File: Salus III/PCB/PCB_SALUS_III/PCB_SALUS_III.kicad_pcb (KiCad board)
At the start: 2 copper layers, 200 x 140 mm, 47 parts, among them J1 Conn_01x20_Pin, J2 Conn_01x20_Pin, K1 Relay_SPDT, U1 ESP32-DEVKITC-32D

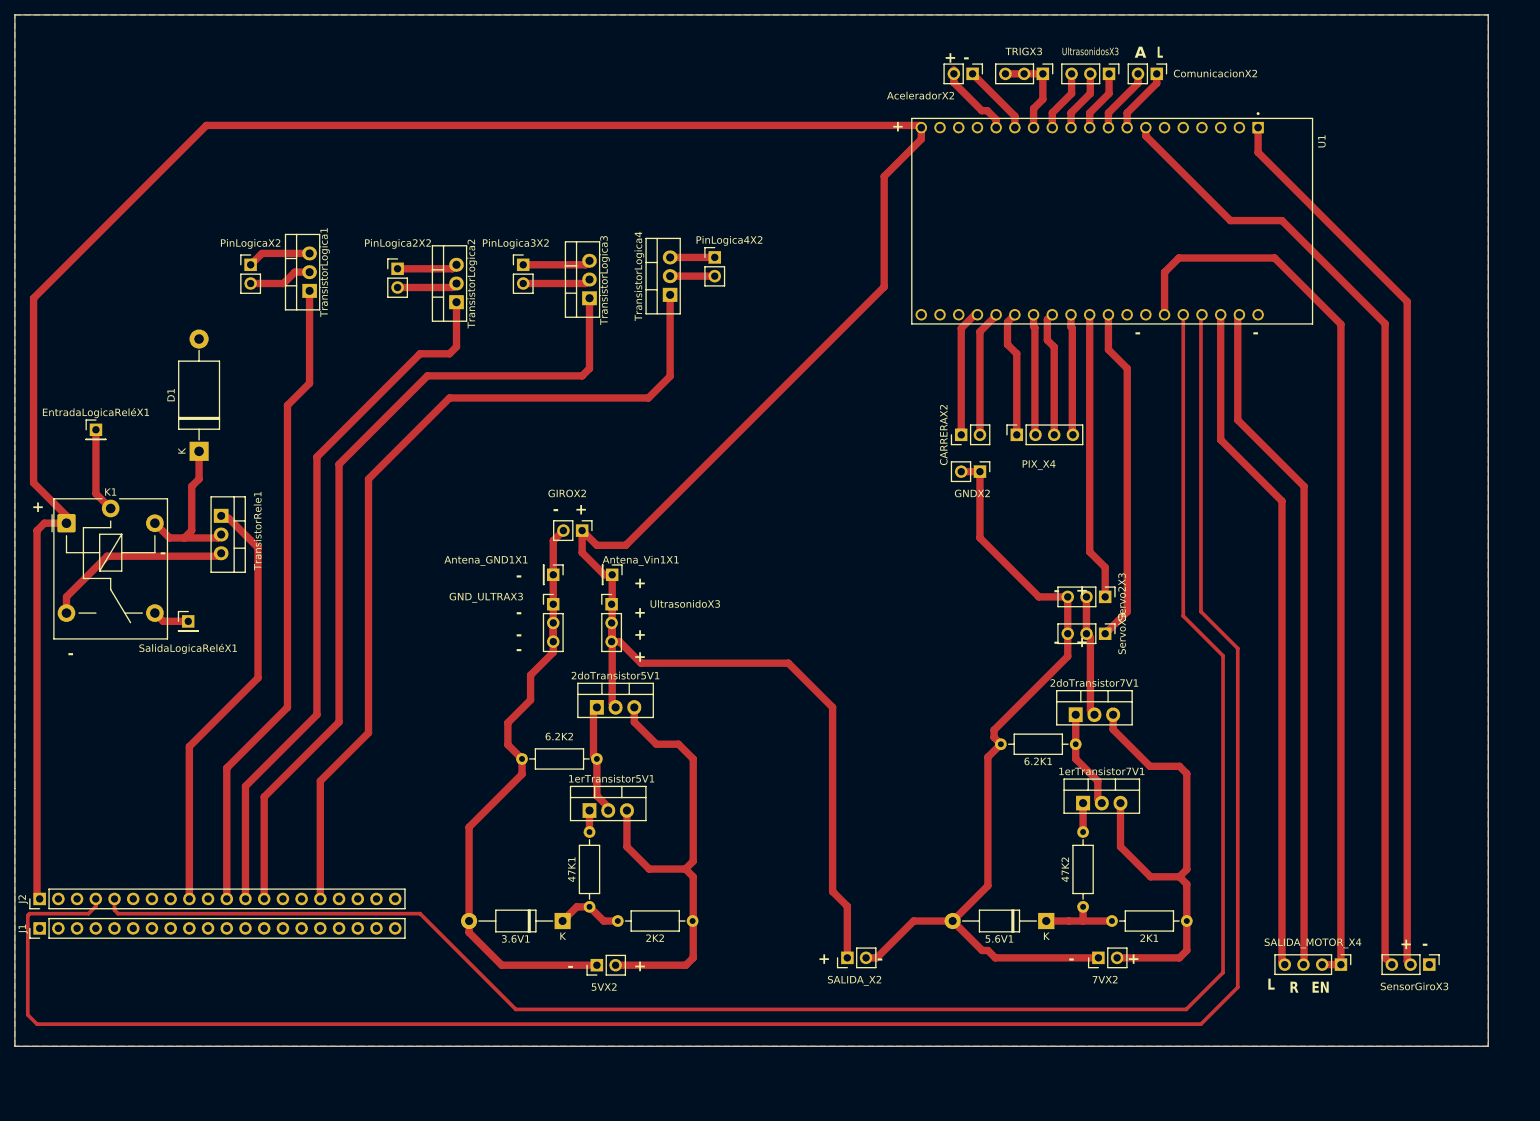
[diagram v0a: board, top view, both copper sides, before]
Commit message: Cambios para realizarla en acido preparados
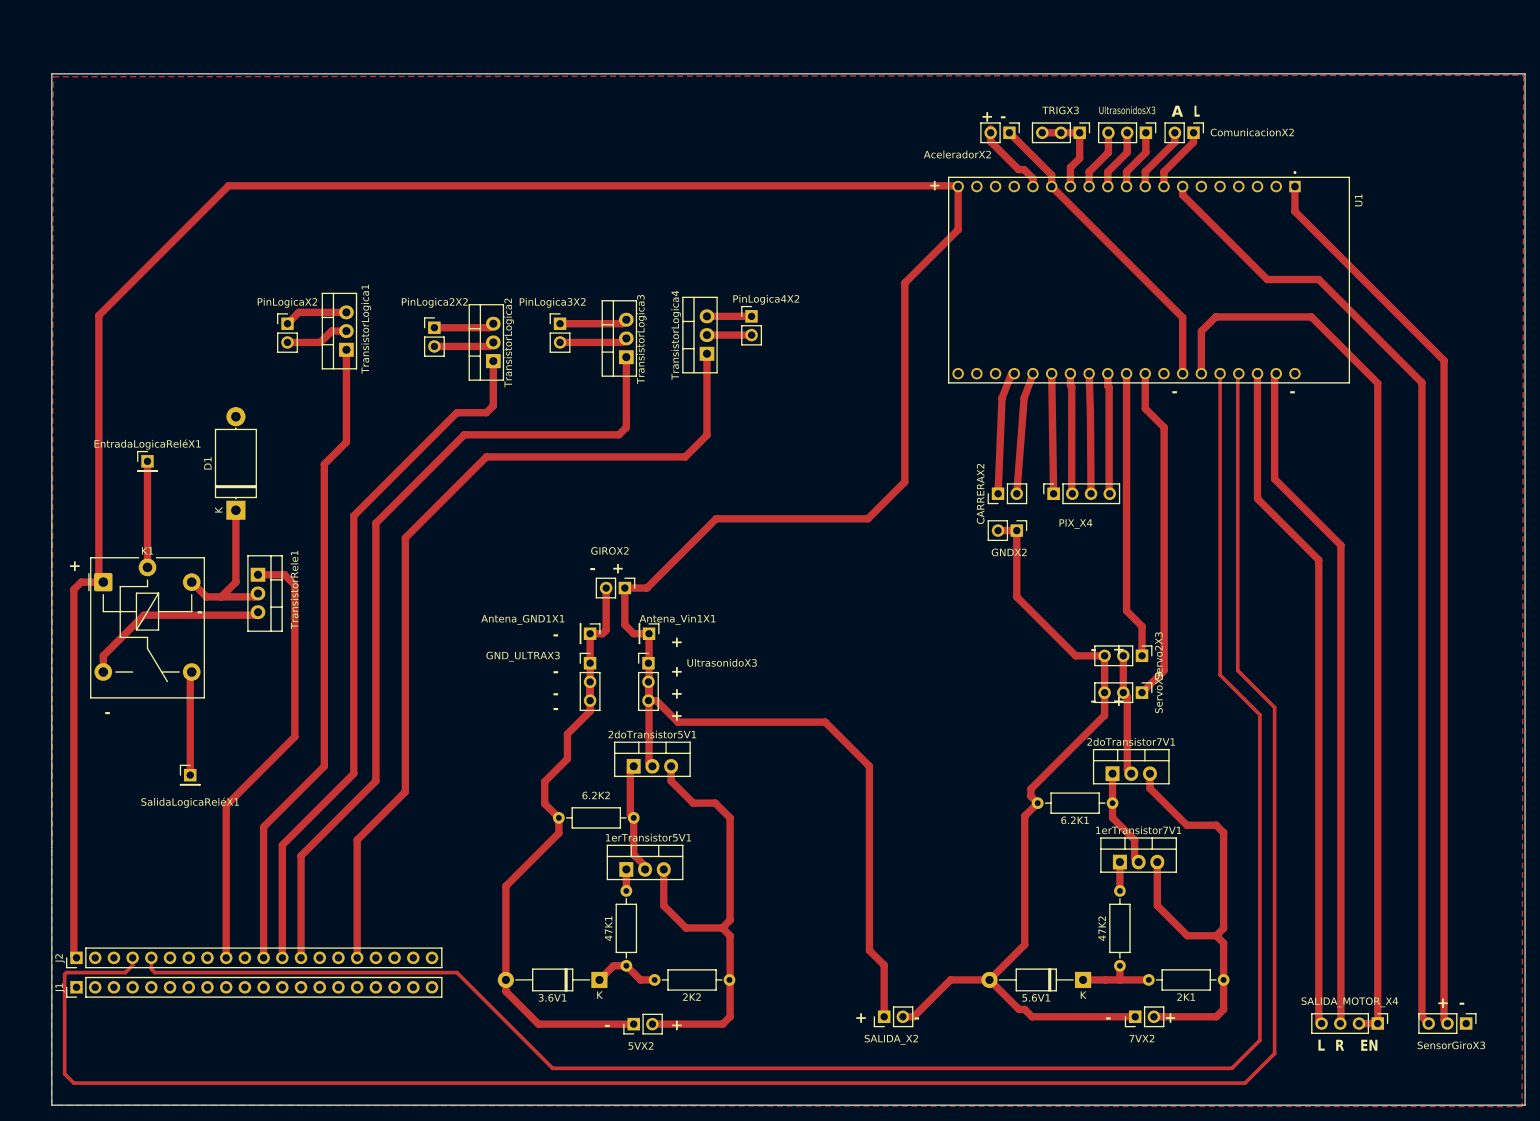
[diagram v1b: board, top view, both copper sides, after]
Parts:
- D1: footprint Diode_THT:D_DO-201AE_P15.24mm_Horizontal -> Diode_THT:D_DO-201AE_P12.70mm_Horizontal
- moved SalidaLogicaReléX1 20.9 mm to (53.8, 125.2)
- moved GIROX2 9.72 mm to (112.8, 99.8)
- moved 1erTransistor5V1 9.43 mm to (113.0, 138.0)
- moved 1erTransistor7V1 9.43 mm to (180.0, 137.0)
- moved 2K1 9.43 mm to (194.1, 153.0)
- moved 2K2 9.43 mm to (127.0, 153.0)
- moved 2doTransistor5V1 9.43 mm to (114.0, 124.0)
- moved 2doTransistor7V1 9.43 mm to (179.0, 125.0)
- moved 3.6V1 9.43 mm to (109.3, 153.0)
- moved 47K1 9.43 mm to (113.0, 151.1)
- moved 47K2 9.43 mm to (180.0, 151.1)
- moved 5.6V1 9.43 mm to (175.0, 153.0)
- moved 5VX2 9.43 mm to (114.0, 159.0)
- moved 6.2K1 9.43 mm to (179.0, 129.0)
- moved 6.2K2 9.43 mm to (114.0, 131.0)
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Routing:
- net GND: track 232.2 -> 266.5 mm
- net Net-(SalidaLogicaReléX1-Pin_1): track 5.00 -> 14.1 mm
- net 5V: track 395.0 -> 400.2 mm
- net Net-(EntradaLogicaReléX1-Pin_1): track 11.5 -> 14.4 mm
- net Net-(J2-Pin_9): track 58.3 -> 60.0 mm
- net Net-(PIX_X4-Pin_1): track 17.2 -> 16.3 mm
- net RX_ESP: track 251.2 -> 251.9 mm
- net Net-(PIX_X4-Pin_3): track 17.0 -> 16.3 mm
- net Net-(CARRERAX2-Pin_2): track 17.2 -> 16.6 mm
- net TX_ESP: track 284.5 -> 285.1 mm
- net Net-(CARRERAX2-Pin_1): track 17.4 -> 16.9 mm
